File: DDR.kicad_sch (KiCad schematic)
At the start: 30 parts

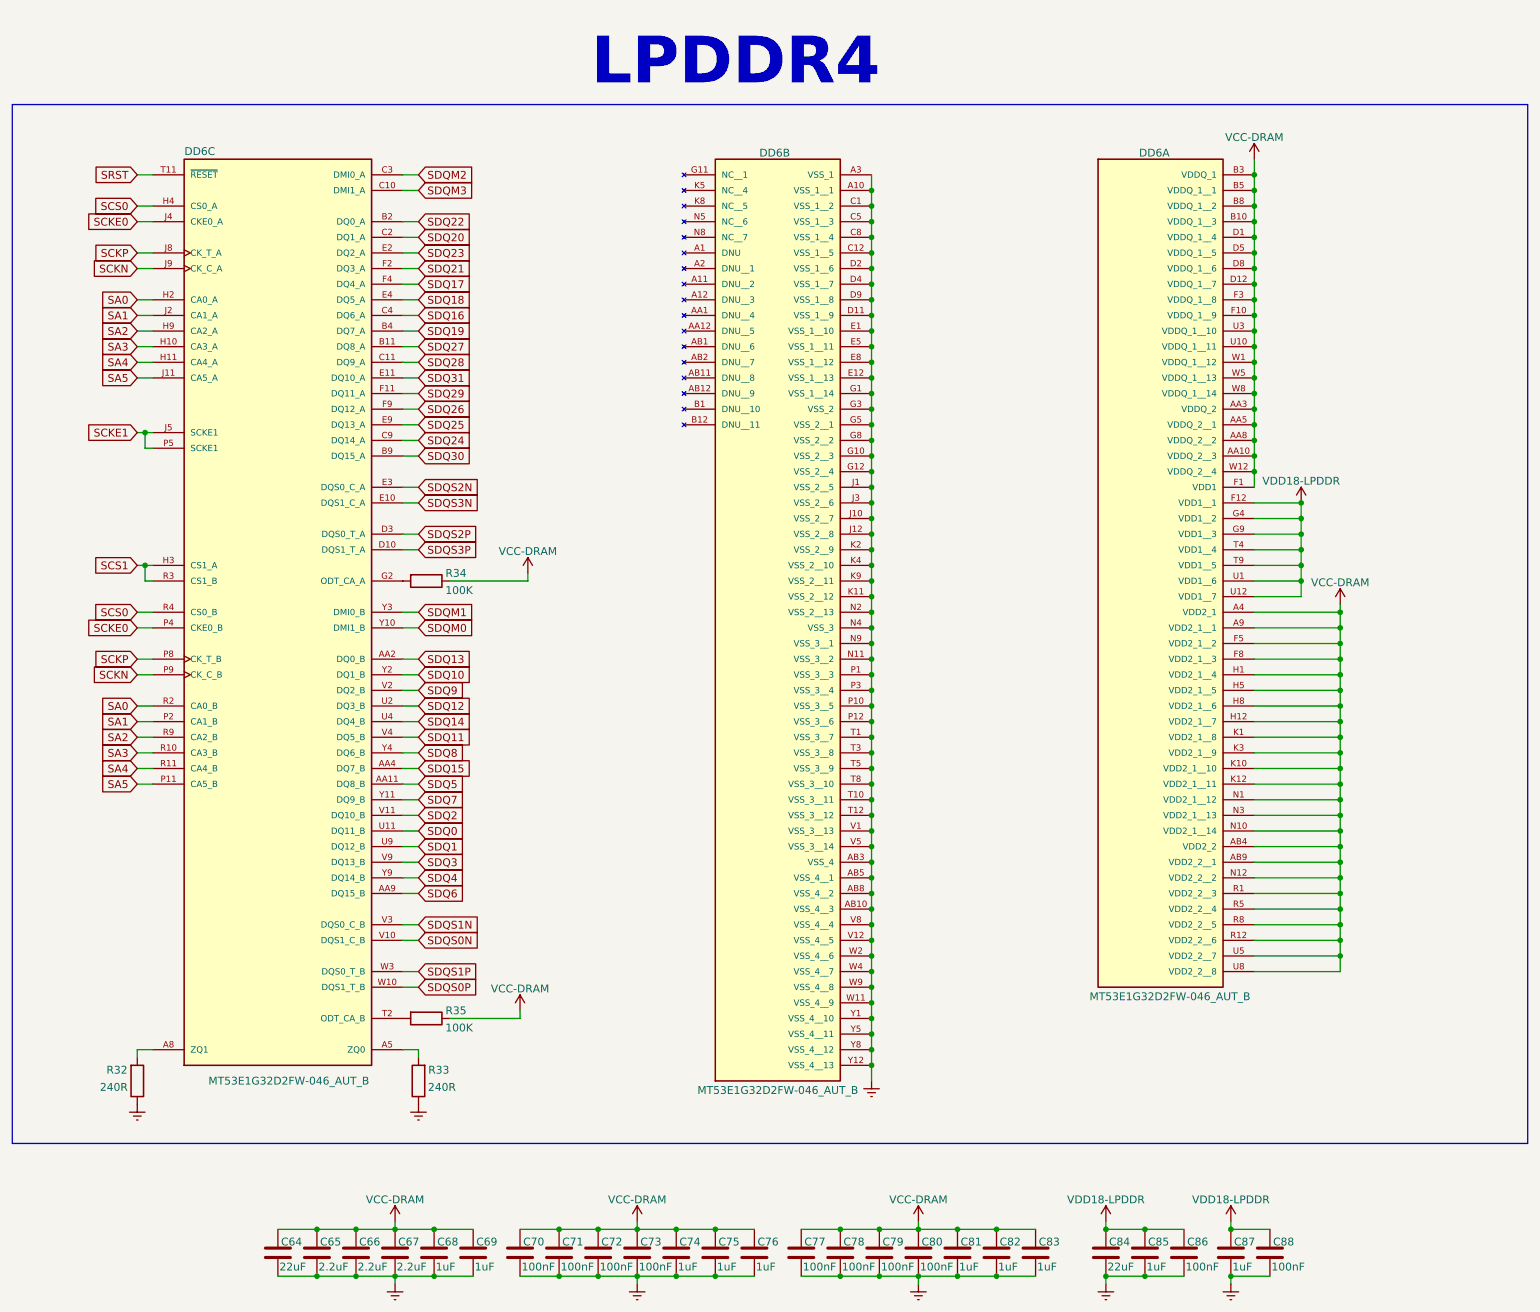
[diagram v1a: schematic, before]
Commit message: Исправление УГО по ГОСТу, добавление 3D моделей
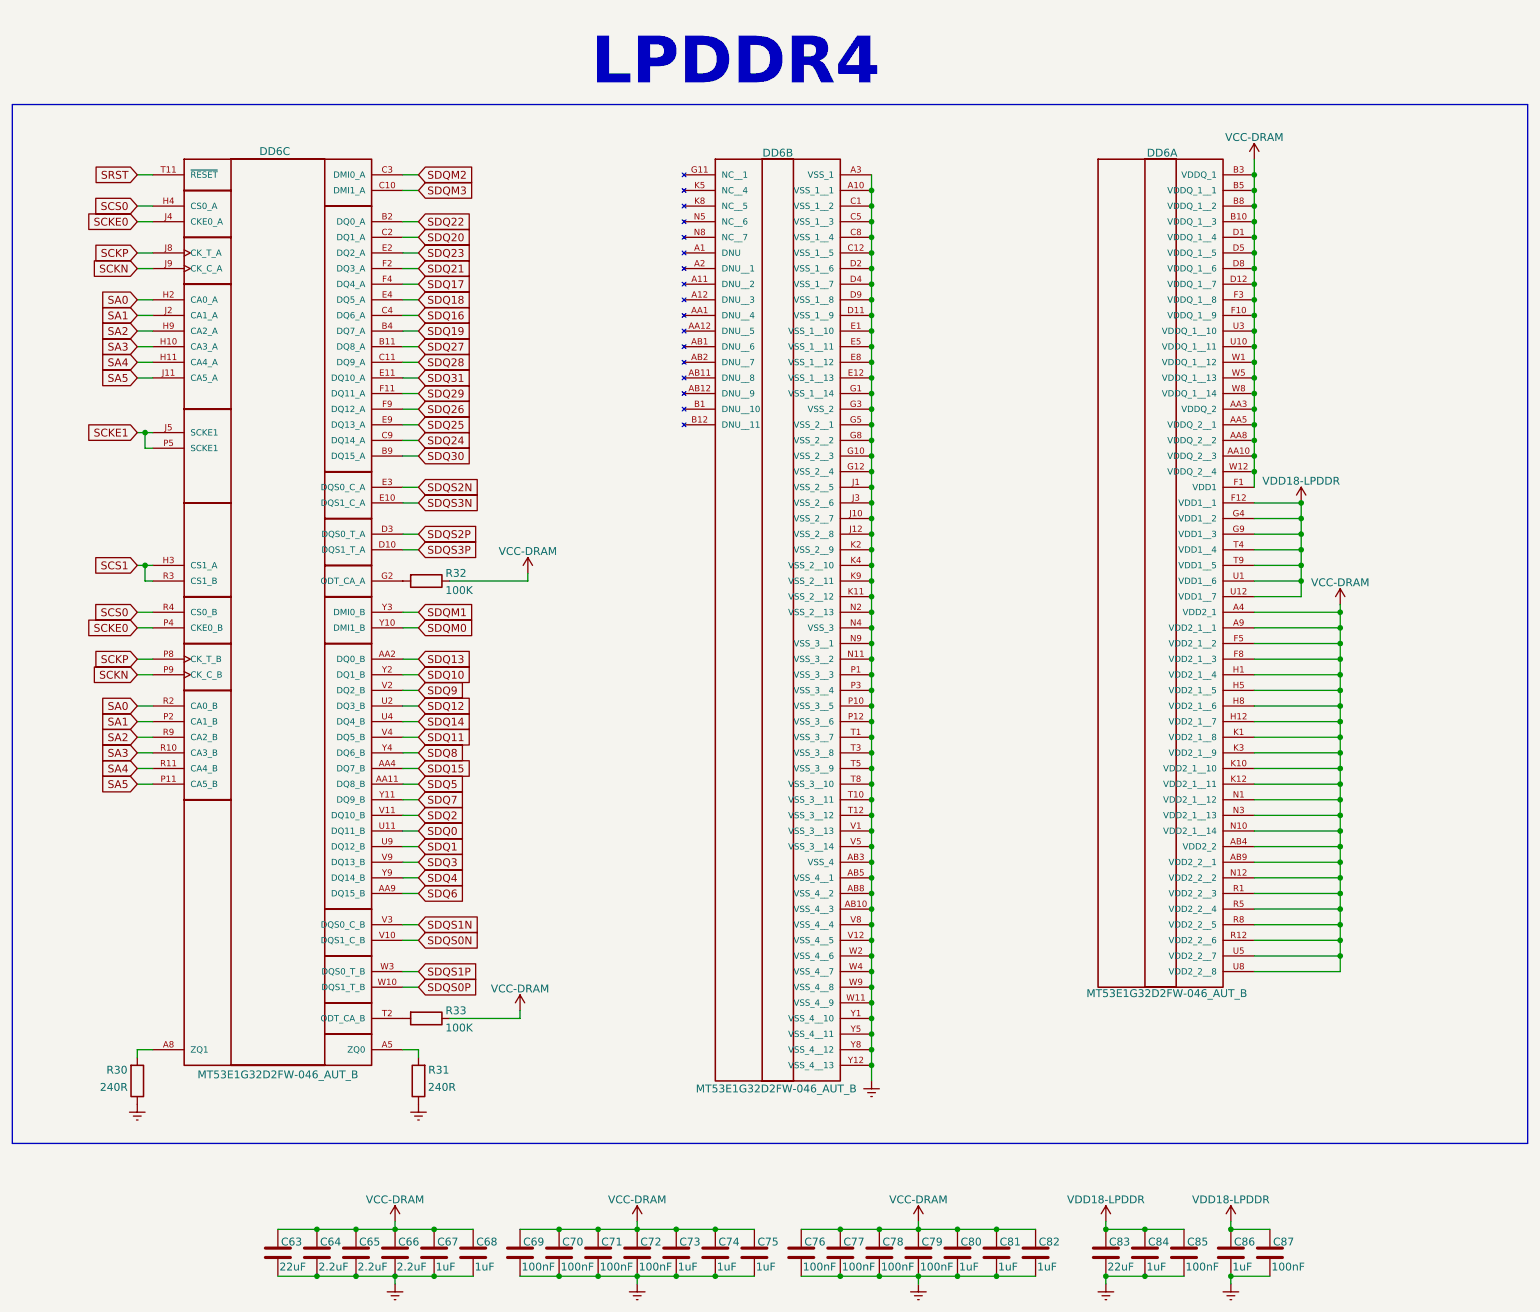
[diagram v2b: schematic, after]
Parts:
- renumbered C64 to C63, C65 to C64, C66 to C65, C67 to C66, C68 to C67, C69 to C68, C70 to C69, C71 to C70, C72 to C71, C73 to C72, C74 to C73, C75 to C74, C76 to C75, C77 to C76, C78 to C77, C79 to C78, C80 to C79, C81 to C80, C82 to C81, C83 to C82, C84 to C83, C85 to C84, C86 to C85, C87 to C86, C88 to C87, R32 to R30, R33 to R31, R34 to R32, R35 to R33
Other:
- company: @madjogger -> РТУ МИРЭА
